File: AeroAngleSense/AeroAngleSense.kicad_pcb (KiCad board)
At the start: 2 copper layers, 15 x 42 mm, 20 parts, among them IC1 STM32F042F6P6, IC2 TMP127EDBVRQ1, IC3 TPS62842DGRR, J1 SM06B-GHS-TBT, J7 SM04B-GHS-TBT

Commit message: pcb layout done.
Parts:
- added H2: MountingHole, MountingHole:MountingHole_2.2mm_M2_Pad, F.Cu at (22.8, 18.0)
- added H3: MountingHole, MountingHole:MountingHole_2.2mm_M2_Pad, F.Cu at (32.2, 18.0)
- added H4: MountingHole, MountingHole:MountingHole_2.2mm_M2_Pad, F.Cu at (32.2, 67.0)
- moved J1 48.3 mm to (33.2, 61.1), turned to 180 degrees
- moved J7 47.6 mm to (24.7, 66.5)
- moved IC3 43.8 mm to (25.7, 59.6)
- moved L1 43.5 mm to (21.5, 58.4), turned to 90 degrees
- moved R3 40.7 mm to (24.2, 62.4), turned to 0 degrees
- moved IC1 40.7 mm to (23.8, 46.0), turned to -90 degrees
- moved H1 40.1 mm to (27.5, 29.4), turned to 0 degrees
- moved C9 37.7 mm to (28.7, 44.0)
- moved C8 37.5 mm to (24.7, 56.6), turned to 0 degrees
- moved C7 35.4 mm to (30.0, 59.2)
- moved R4 35.1 mm to (34.0, 44.8)
- moved IC2 32.2 mm to (31.4, 44.0), turned to 90 degrees
- moved R1 30.5 mm to (26.8, 40.5)
- moved C1 21.1 mm to (23.5, 39.8), turned to 180 degrees
- moved C2 20.4 mm to (23.5, 41.2), turned to 180 degrees
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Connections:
- H1 pad 2: unconnected-(H1-WIPER_-Pad2) -> Net-(H1-WIPER_)
- H1 pad A2: Net-(H1-WIPER) -> unconnected-(H1-WIPER-PadA2)
- R2 pad 1: Net-(H1-WIPER) -> Net-(H1-WIPER_)
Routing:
- net /TMP_CS: track 27.7 -> 0.00 mm
- net +5V: track 19.9 -> 0.00 mm
- net /TMP_MISO: track 17.5 -> 0.00 mm
- net /TMP_SCLK: track 17.3 -> 0.00 mm
- net GND: track 16.0 -> 6.01 mm, vias 0 -> 8
- net Net-(IC3-SW): track 4.95 -> 0.00 mm
- net Net-(IC3-VSET): track 3.06 -> 0.00 mm
- net /TMP_MOSI: track 2.12 -> 0.00 mm
- net +3.3V: track 9.51 -> 9.41 mm, vias 0 -> 1
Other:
- board size 15 x 42 mm -> 15 x 55 mm

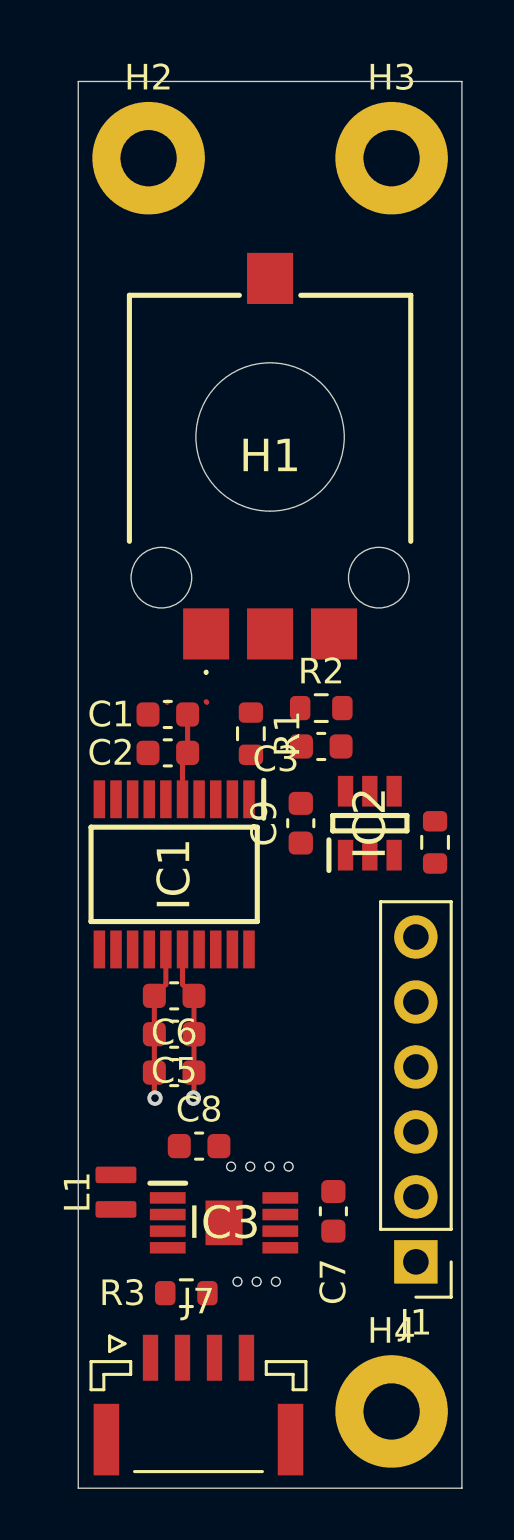
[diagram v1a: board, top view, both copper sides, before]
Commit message: add : copper zone"
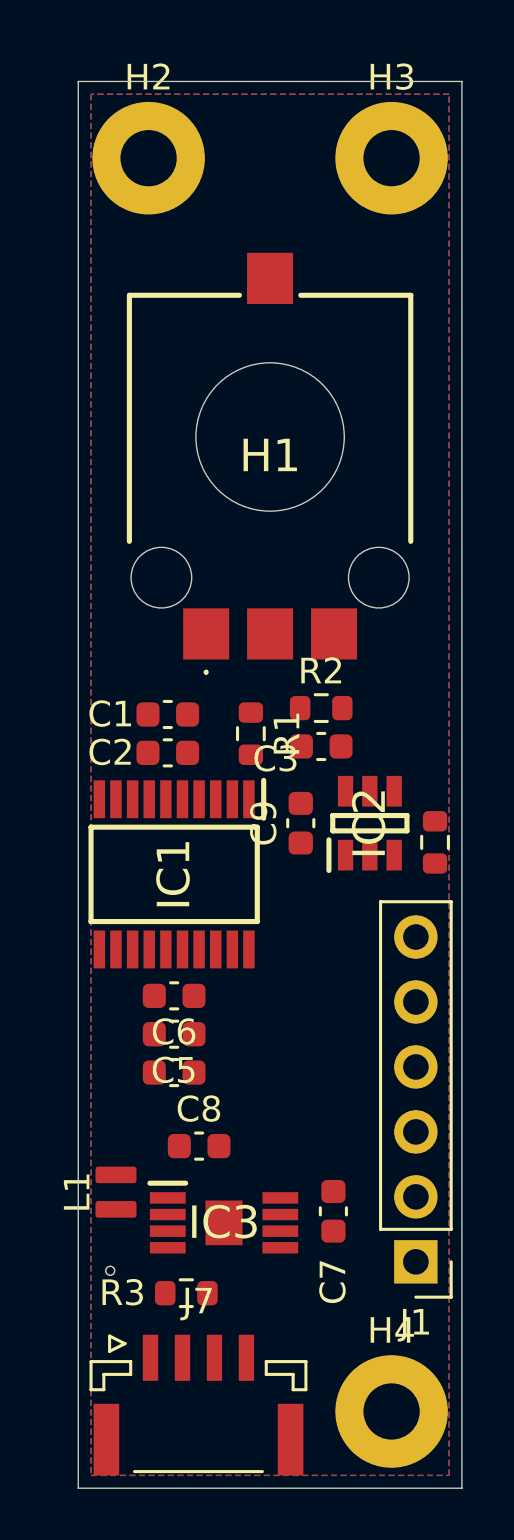
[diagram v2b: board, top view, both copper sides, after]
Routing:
- net +3.3V: track 9.41 -> 0.00 mm, vias 1 -> 0
- net GND: track 6.01 -> 0.00 mm, vias 8 -> 1
- added copper zone on B.Cu, net GND
- added copper zone on F.Cu, net GND
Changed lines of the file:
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@@
 		(layer "User.1")
 	)
-	(segment
-		(start 22.975 53.75)
-		(end 22.975 54.725)
-		(width 0.2)
-		(layer "F.Cu")
-		(net 1)
-	)
-	(segment
-		(start 23.425 48.935)
-		(end 23.425 50.3)
-		(width 0.2)
-		(layer "F.Cu")
-		(net 1)
-	)
-	(segment
-		(start 25.025 39.275)
-		(end 25 39.25)
-		(width 0.2)
-		(layer "F.Cu")
-		(net 1)
-	)
-	(segment
-		(start 22.975 53.75)
-		(end 22.975 50.75)
-		(width 0.2)
-		(layer "F.Cu")
-		(net 1)
-	)
-	(segment
-		(start 23.425 50.3)
-		(end 22.975 50.75)
-		(width 0.2)
-		(layer "F.Cu")
-		(net 1)
-	)
 	(via
-		(at 27.725 61.925)
+		(at 21.25 61.5)
 		(size 0.4)
 		(drill 0.3)
 		(layers "F.Cu" "B.Cu")
+		(free yes)
 		(net 1)
 	)
-	(via
-		(at 27.475 57.425)
-		(size 0.4)
-		(drill 0.3)
+	(zone
+		(net 0)
+		(net_name "")
+		(layer "F.Cu")
+		(hatch edge 0.5)
+		(connect_pads
+			(clearance 0)
+		)
+		(min_thickness 0.25)
+		(filled_areas_thickness no)
+		(keepout
+			(tracks allowed)
+			(vias allowed)
+			(pads allowed)
+			(copperpour not_allowed)
+			(footprints allowed)
+		)
+		(placement
+			(enabled no)
+			(sheetname "/")
+		)
+		(fill
+			(thermal_gap 0.5)
+			(thermal_bridge_width 0.5)
+		)
+		(polygon
+			(pts
+				(xy 22.25 50) (xy 22.25 55) (xy 25.25 55) (xy 25.25 50)
+			)
+		)
+	)
+	(zone
+		(net 1)
+		(net_name "GND")
 		(layers "F.Cu" "B.Cu")
-		(net 1)
-	)
-	(via
-		(at 28.225 57.425)
-		(size 0.4)
-		(drill 0.3)
-		(layers "F.Cu" "B.Cu")
-		(net 1)
-	)
-	(via
-		(at 26.975 61.925)
-		(size 0.4)
-		(drill 0.3)
-		(layers "F.Cu" "B.Cu")
-		(net 1)
-	)
-	(via
-		(at 25.975 57.425)
-		(size 0.4)
-		(drill 0.3)
-		(layers "F.Cu" "B.Cu")
-		(net 1)
-	)
-	(via
-		(at 26.225 61.925)
-		(size 0.4)
-		(drill 0.3)
-		(layers "F.Cu" "B.Cu")
-		(net 1)
-	)
-	(via
-		(at 26.725 57.425)
-		(size 0.4)
-		(drill 0.3)
-		(layers "F.Cu" "B.Cu")
-		(net 1)
-	)
-	(via
-		(at 23 54.75)
-		(size 0.6)
-		(drill 0.3)
-		(layers "F.Cu" "B.Cu")
-		(net 1)
-	)
-	(segment
-		(start 24.075 43.065)
-		(end 24.075 41.45)
-		(width 0.2)
-		(layer "F.Cu")
-		(net 2)
-	)
-	(segment
-		(start 24.075 50.3)
-		(end 24.525 50.75)
-		(width 0.2)
-		(layer "F.Cu")
-		(net 2)
-	)
-	(segment
-		(start 23.475 39.275)
-		(end 23.5 39.25)
-		(width 0.2)
-		(layer "F.Cu")
-		(net 2)
-	)
-	(segment
-		(start 24.525 53.75)
-		(end 24.525 50.75)
-		(width 0.2)
-		(layer "F.Cu")
-		(net 2)
-	)
-	(segment
-		(start 24.525 53.75)
-		(end 24.525 54.725)
-		(width 0.2)
-		(layer "F.Cu")
-		(net 2)
-	)
-	(segment
-		(start 24.275 41.25)
-		(end 24.275 39.75)
-		(width 0.2)
-		(layer "F.Cu")
-		(net 2)
-	)
-	(segment
-		(start 24.075 41.45)
-		(end 24.275 41.25)
-		(width 0.2)
-		(layer "F.Cu")
-		(net 2)
-	)
-	(segment
-		(start 24.075 48.935)
-		(end 24.075 50.3)
-		(width 0.2)
-		(layer "F.Cu")
-		(net 2)
-	)
-	(via
-		(at 24.5 54.75)
-		(size 0.6)
-		(drill 0.3)
-		(layers "F.Cu" "B.Cu")
-		(net 2)
+		(hatch edge 0.5)
+		(connect_pads
+			(clearance 0.5)
+		)
+		(min_thickness 0.25)
+		(filled_areas_thickness no)
+		(fill yes
+			(thermal_gap 0.5)
+			(thermal_bridge_width 0.5)
+		)
+		(polygon
+			(pts
+				(xy 20.5 69.5) (xy 34.5 69.5) (xy 34.5 15.5) (xy 20.5 15.5)
+			)
+		)
 	)
 	(embedded_fonts no)
